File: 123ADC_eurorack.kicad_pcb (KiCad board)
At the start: 2 copper layers, 90 x 128.5 mm, 77 parts, among them J1 CLOCK_IN, J10 BIT_7, J11 Conn_01x06_Male, J12 Conn_01x06_Female, J13 Conn_01x06_Male, J14 Conn_01x06_Female, J15 Conn_02x05_Odd_Even, J2 CV_IN, J3 BIT_0, J4 BIT_1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

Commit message: :sparkles: Add reverse power protection and power conditioning caps
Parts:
- added C1: 10uF, Capacitor_THT:CP_Radial_D5.0mm_P2.50mm, F.Cu at (138.8, 105.8)
- added C2: 100nF, Capacitor_THT:C_Disc_D3.8mm_W2.6mm_P2.50mm, F.Cu at (153.0, 66.5)
- added D3: 1N5817, Diode_THT:D_DO-41_SOD81_P10.16mm_Horizontal, F.Cu at (140.0, 110.2)
- D4, D5, D6, D7, D8: value 48 -> 1N4148
- U1: value REG1117-5 -> REG1117
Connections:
- J15 pad 1: +12V -> Net-(D3-Pad2)
- J15 pad 2: +12V -> Net-(D3-Pad2)
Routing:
- net Net-(D3-Pad2): track 0.00 -> 5.69 mm
- net +5V: track 86.7 -> 90.6 mm
- net /BIT_7: track 87.0 -> 90.0 mm
- net /BIT_6: track 80.7 -> 83.4 mm
- net Net-(D1-Pad1): track 65.7 -> 67.8 mm
- net +12V: track 11.7 -> 12.8 mm

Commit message: :sparkles: Add graphics for output numbers, and LMNC logo
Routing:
- net /HEATSINK: vias 41 -> 57

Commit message: :sparkles: Name in handwriting
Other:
- board text removed: "123ADC"

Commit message: :recycle: Clean up silkscreen
same
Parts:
- D4, D5, D6, D7, D8: value 1N4148 -> 48
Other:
- board text added: "ADC123 Panel v1.0 nebularnoise.com"
- board text added: "ADC123 bottom pcb v1.0 nebularnoise.com"
- board text added: "ADC123 top pcb v1.0 nebularnoise.com"
- board text added: "JLCJLCJLCJLC"
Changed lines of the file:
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@@
   (general
     (thickness 1.6)
-    (drawings 680)
+    (drawings 686)
     (tracks 291)
     (zones 0)
@@
       (effects (font (size 1 1) (thickness 0.15)))
     )
-    (fp_text value 1N4148 (at 4 0 270) (layer F.SilkS)
+    (fp_text value 48 (at 4 0 270) (layer F.SilkS)
       (effects (font (size 1 1) (thickness 0.15)))
     )
@@
       (effects (font (size 1 1) (thickness 0.15)))
     )
-    (fp_text value 1N4148 (at 4 0 270) (layer F.SilkS)
+    (fp_text value 48 (at 4 0 270) (layer F.SilkS)
       (effects (font (size 1 1) (thickness 0.15)))
     )
@@
       (effects (font (size 1 1) (thickness 0.15)))
     )
-    (fp_text value 1N4148 (at 4 0 270) (layer F.SilkS)
+    (fp_text value 48 (at 4 0 270) (layer F.SilkS)
       (effects (font (size 1 1) (thickness 0.15)))
     )
@@
       (effects (font (size 1 1) (thickness 0.15)))
     )
-    (fp_text value 1N4148 (at 4 0 270) (layer F.SilkS)
+    (fp_text value 48 (at 4 0 270) (layer F.SilkS)
       (effects (font (size 1 1) (thickness 0.15)))
     )
@@
       (effects (font (size 1 1) (thickness 0.15)))
     )
-    (fp_text value 1N4148 (at 4 0 270) (layer F.SilkS)
+    (fp_text value 48 (at 4 0 270) (layer F.SilkS)
       (effects (font (size 1 1) (thickness 0.15)))
     )
@@
       (effects (font (size 1 1) (thickness 0.15)))
     )
-    (fp_text value 1k (at 3.81 2.37 90) (layer F.Fab)
+    (fp_text value 1k (at 5.925 -0.475 180) (layer F.SilkS)
       (effects (font (size 1 1) (thickness 0.15)))
     )
@@
       (effects (font (size 1 1) (thickness 0.15)))
     )
-    (fp_text value 1k (at 3.81 2.37 90) (layer F.Fab)
+    (fp_text value 1k (at 6 0.425 180) (layer F.SilkS)
       (effects (font (size 1 1) (thickness 0.15)))
     )
@@
     (descr "Through hole straight pin header, 1x06, 2.54mm pitch, single row")
     (tags "Through hole pin header THT 1x06 2.54mm single row")
-    (fp_text reference J11 (at 0 2.33 90) (layer B.SilkS)
+    (fp_text reference J11 (at 0 2.33 90) (layer B.SilkS) hide
       (effects (font (size 1 1) (thickness 0.15)) (justify mirror))
     )
@@
     (descr "Through hole straight pin header, 1x06, 2.54mm pitch, single row")
     (tags "Through hole pin header THT 1x06 2.54mm single row")
-    (fp_text reference J13 (at 0 2.33 90) (layer B.SilkS)
+    (fp_text reference J13 (at 0 2.33 90) (layer B.SilkS) hide
       (effects (font (size 1 1) (thickness 0.15)) (justify mirror))
     )
@@
     )
   )
+  (gr_text "ADC123\nbottom pcb v1.0\nnebularnoise.com" (at 145.8 142.225) (layer F.SilkS)
+    (effects (font (size 1 1) (thickness 0.15)))
+  )
+  (gr_text "ADC123 top pcb v1.0\nnebularnoise.com" (at 111.874999 67.025 90) (layer B.SilkS)
+    (effects (font (size 1 1) (thickness 0.15)) (justify mirror))
+  )
+  (gr_text JLCJLCJLCJLC (at 137.25 142.725001 90) (layer F.SilkS)
+    (effects (font (size 1 1) (thickness 0.15)))
+  )
+  (gr_text JLCJLCJLCJLC (at 114.075 141.35) (layer B.SilkS)
+    (effects (font (size 1 1) (thickness 0.15)) (justify mirror))
+  )
+  (gr_text JLCJLCJLCJLC (at 75.75 160.725) (layer B.SilkS)
+    (effects (font (size 1 1) (thickness 0.15)) (justify mirror))
+  )
+  (gr_text "ADC123 Panel v1.0\nnebularnoise.com" (at 75.75 51.1) (layer B.SilkS)
+    (effects (font (size 1 1) (thickness 0.15)) (justify mirror))
+  )
   (gr_curve (pts (xy 81.176162 50.807688) (xy 81.090263 50.847913) (xy 81.000187 50.882719) (xy 80.910207 50.916281)) (layer F.Mask) (width 0.01))

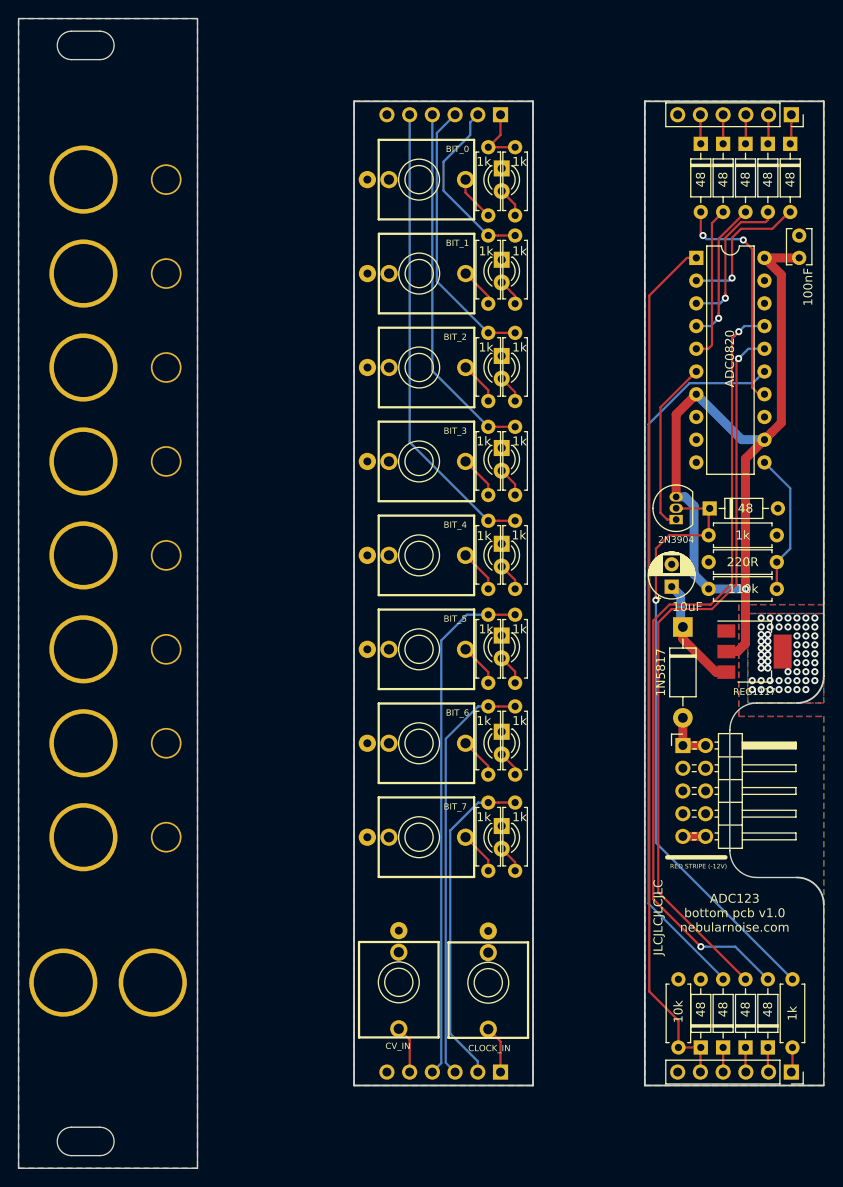
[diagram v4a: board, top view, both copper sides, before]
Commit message: :bug: Fix resistor values
same
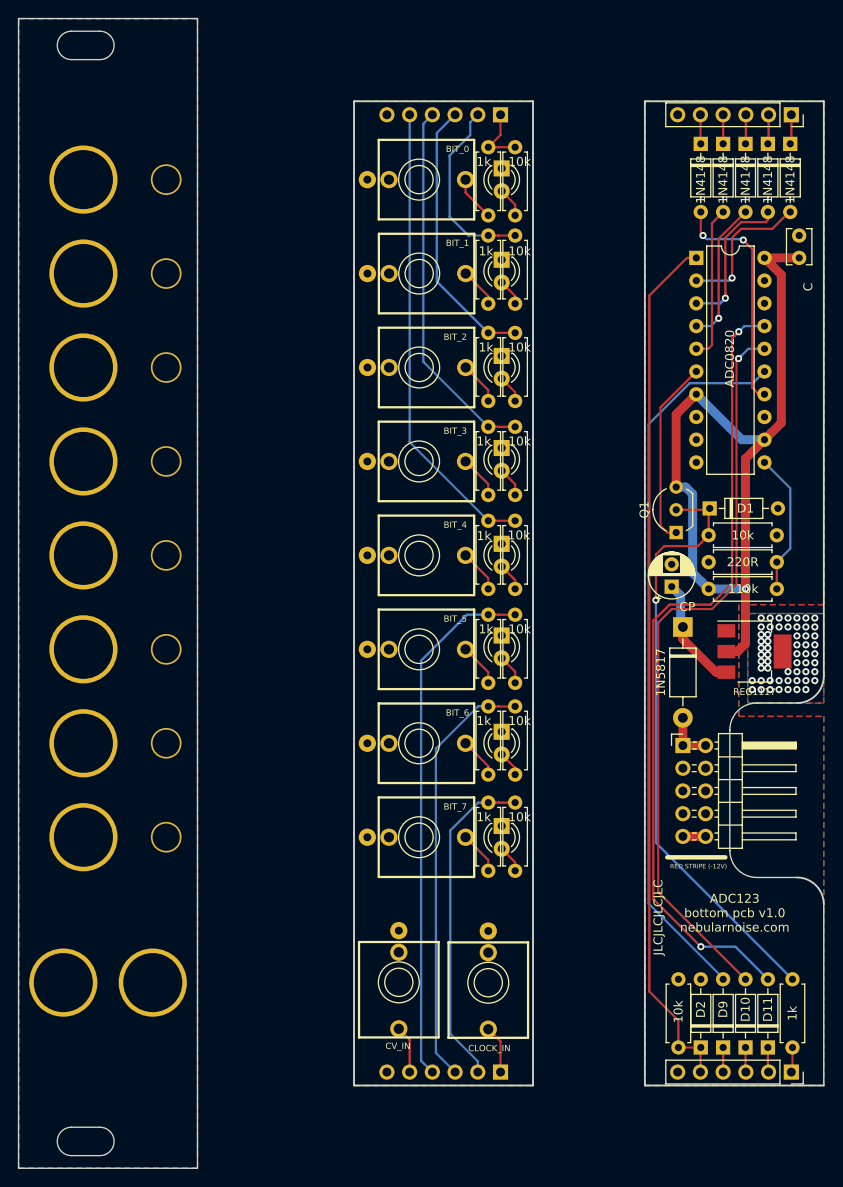
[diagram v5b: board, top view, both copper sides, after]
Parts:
- C1: value 10uF -> CP
- C2: value 100nF -> C
- D4, D5, D6, D7, D8: value 48 -> 1N4148
- Q1: footprint Package_TO_SOT_THT:TO-92_Inline -> Package_TO_SOT_THT:TO-92_Inline_Wide
- R10, R12, R14, R16, R18, R2, R20, R22, R8: value 1k -> 10k
- moved Q1 1.44 mm to (139.2, 99.7)
- renumbered 48 to D1, 48 to D10, 48 to D11, 48 to D2, 48 to D9
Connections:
- J1 pad TN: (no net) -> Net-(J1-PadTN)
- J10 pad TN: (no net) -> Net-(J10-PadTN)
- J2 pad TN: (no net) -> Net-(J2-PadTN)
- J3 pad TN: (no net) -> Net-(J3-PadTN)
- J4 pad TN: (no net) -> Net-(J4-PadTN)
- J5 pad TN: (no net) -> Net-(J5-PadTN)
- J6 pad TN: (no net) -> Net-(J6-PadTN)
- J7 pad TN: (no net) -> Net-(J7-PadTN)
- J8 pad TN: (no net) -> Net-(J8-PadTN)
- J9 pad TN: (no net) -> Net-(J9-PadTN)
- U3 pad 18: (no net) -> Net-(U3-Pad18)
- U3 pad 19: (no net) -> Net-(U3-Pad19)
- U3 pad 9: (no net) -> Net-(U3-Pad9)
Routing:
- net Net-(Q1-Pad1): track 19.5 -> 21.0 mm
- net /BIT_5_D__: track 58.1 -> 59.1 mm
- net /BIT_6_D__: track 46.9 -> 47.8 mm
- net /BIT_3_D__: track 40.5 -> 41.3 mm
- net /BIT_1_D__: track 20.2 -> 20.9 mm
